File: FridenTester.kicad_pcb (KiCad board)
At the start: 4 copper layers, 18.5 x 40.4 mm, 22 parts, among them P1 CONN_02X05, U1 BSD223P, U10 BSD223P, U11 BSD223P, U12 2N7002DN, U13 2N7002DN, U14 BSD223P, U15 BSD223P, U16 2N7002DN, U17 2N7002DN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

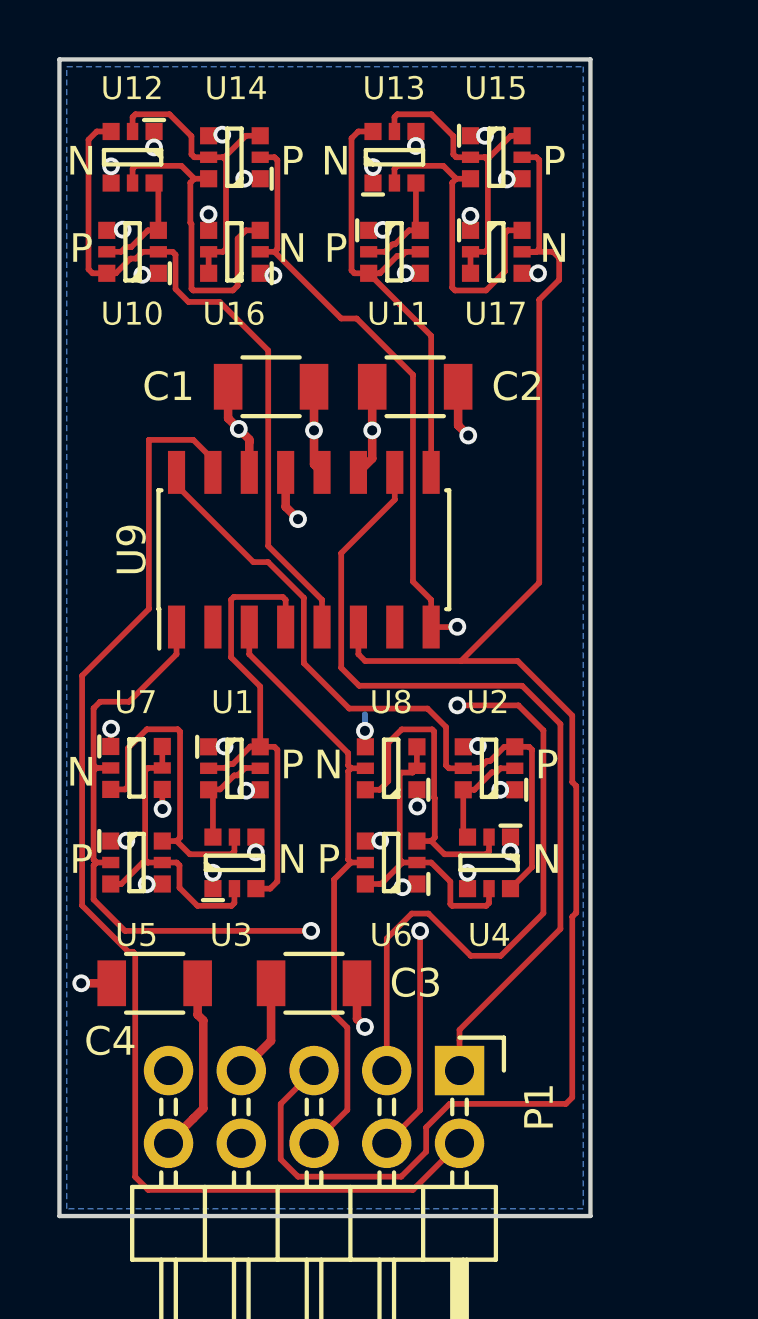
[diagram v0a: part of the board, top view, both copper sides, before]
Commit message: Version B (version A had bad pinouts for NMOS)
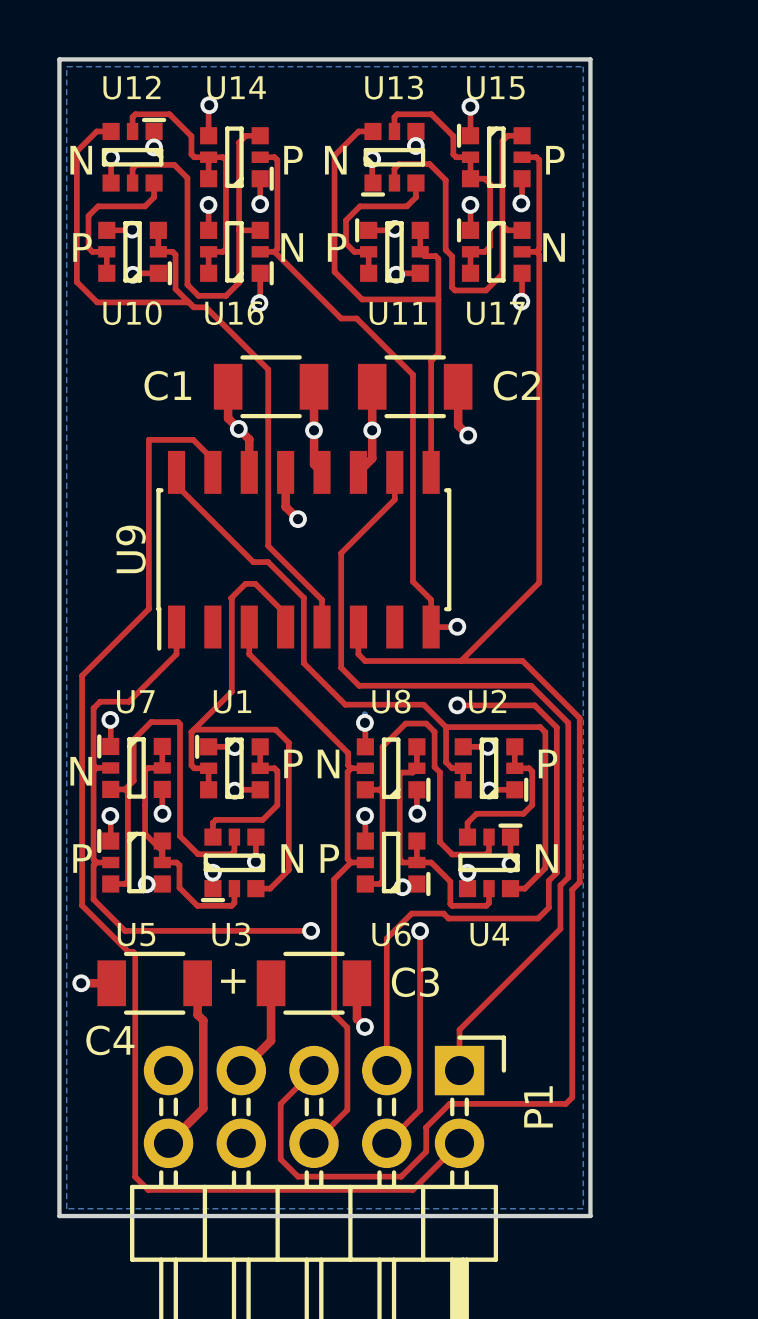
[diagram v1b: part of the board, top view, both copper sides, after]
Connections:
- U1 pad 3: /-OUT5A -> /OUT5A
- U1 pad 6: /OUT5A -> /-OUT5A
- U10 pad 3: /-OUT5B -> /OUT5B
- U10 pad 6: /OUT5B -> /-OUT5B
- U11 pad 3: /OUT12B -> /-OUT12B
- U11 pad 6: /-OUT12B -> /OUT12B
- U14 pad 3: /-IN12B -> /IN12B_BUF
- U14 pad 6: /IN12B_BUF -> /-IN12B
- U15 pad 3: /IN5B_BUF -> /-IN5B
- U15 pad 6: /-IN5B -> /IN5B_BUF
- U2 pad 3: /OUT12A -> /-OUT12A
- U2 pad 6: /-OUT12A -> /OUT12A
- U5 pad 3: /-IN12A -> /IN12A_BUF
- U5 pad 6: /IN12A_BUF -> /-IN12A
- U6 pad 3: /IN5A_BUF -> /-IN5A
- U6 pad 6: /-IN5A -> /IN5A_BUF
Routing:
- net GNDREF: track 19.2 -> 23.3 mm
- net /OUT5A: track 16.7 -> 20.5 mm
- net /IN12A_BUF: track 11.2 -> 14.8 mm
- net /IN12B_BUF: track 11.6 -> 15.0 mm
- net /IN5A_BUF: track 11.2 -> 14.6 mm
- net /IN5B_BUF: track 11.4 -> 14.6 mm
- net /OUT12B: track 16.1 -> 19.0 mm
- net +12V: track 13.6 -> 16.4 mm
- net /OUT5B: track 24.6 -> 27.3 mm
- net /OUT12A: track 24.6 -> 27.2 mm
- net VDD: track 11.1 -> 13.6 mm
- net /-OUT5B: track 3.82 -> 5.83 mm
- net /-OUT12A: track 3.82 -> 5.81 mm
- net /-OUT12B: track 3.82 -> 5.74 mm
- net /-OUT5A: track 3.82 -> 5.58 mm
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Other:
- board text added: "+"
- board text added: "0"
- board text added: "1"
- board text added: "REV B 28 OCT 2016"
- board text removed: "REV A 12 OCT 2016"
